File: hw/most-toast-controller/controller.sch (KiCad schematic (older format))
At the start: 1 part

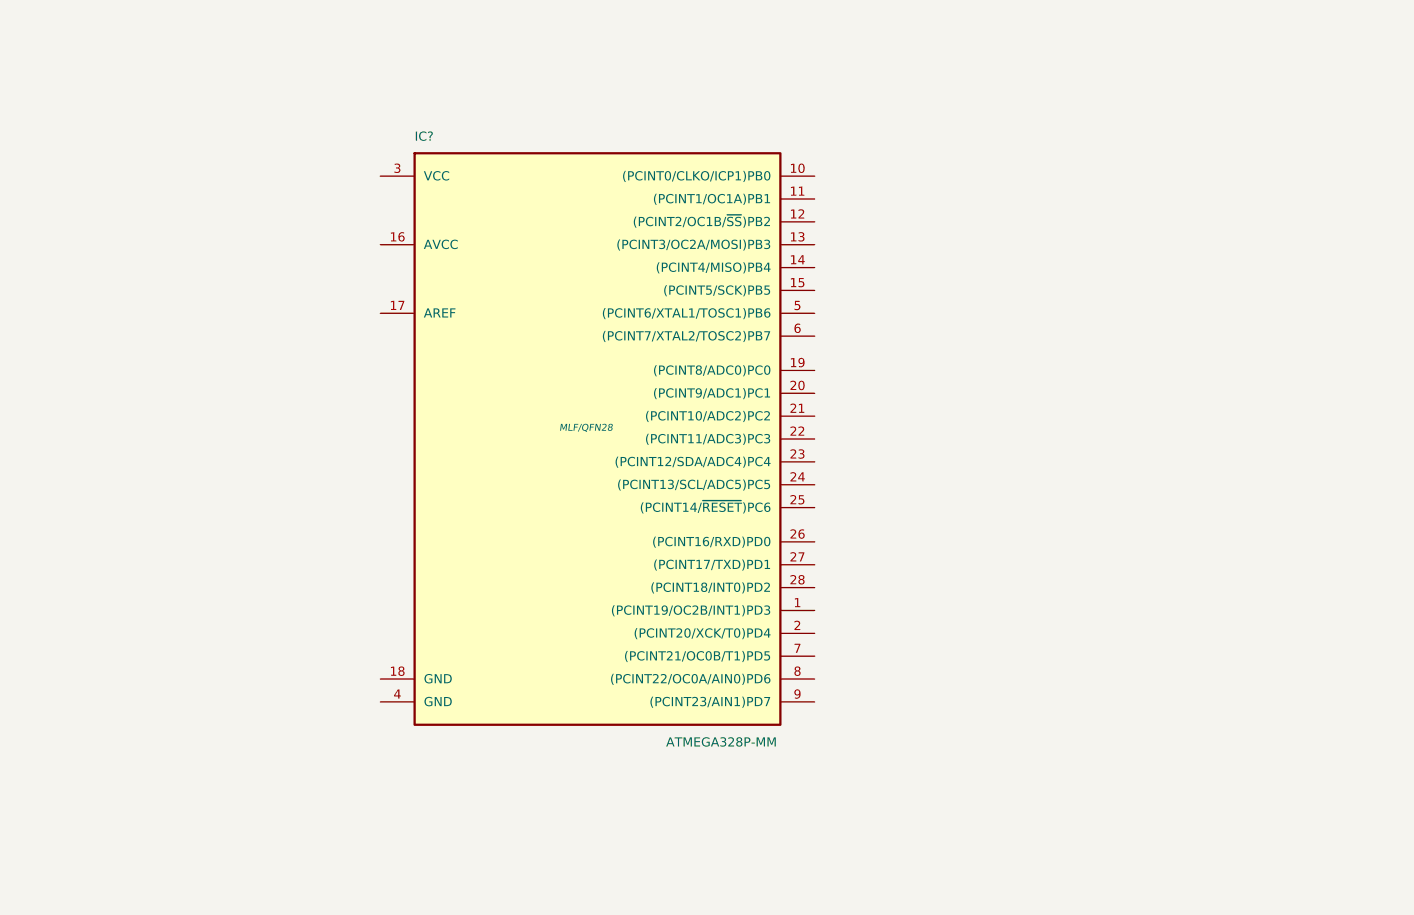
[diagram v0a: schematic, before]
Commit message: most-toast schematic finished.
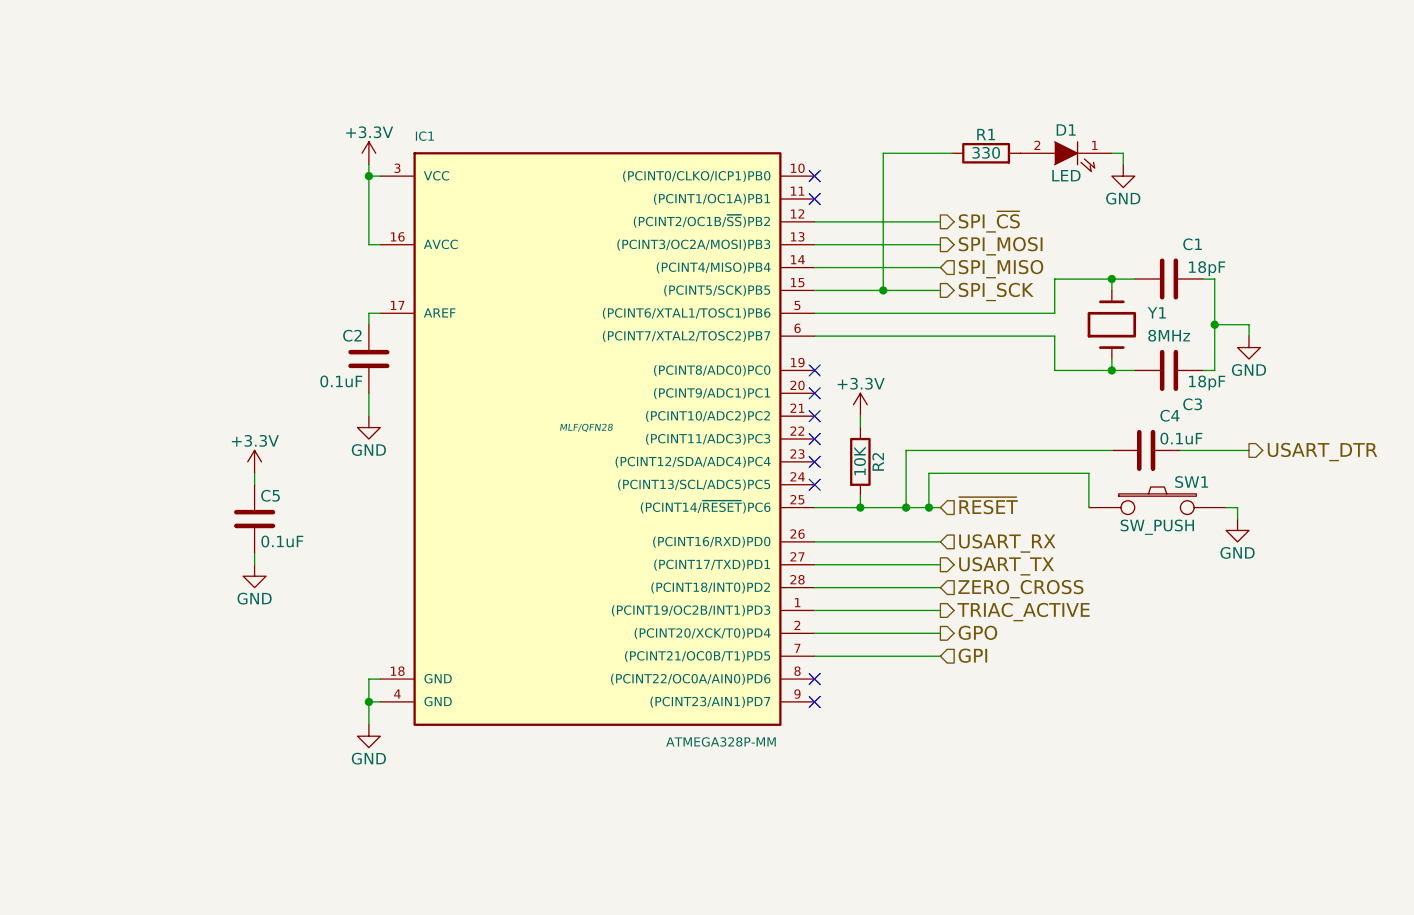
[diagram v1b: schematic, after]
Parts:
- added C1, C3: 18pF, symbol C
- added C2, C4, C5: 0.1uF, symbol C
- added D1: LED, symbol LED
- added R1: 330, symbol R
- added R2: 10K, symbol R
- added SW1: SW_PUSH, symbol SW_PUSH
- added Y1: 8MHz, symbol Crystal
- gave numbers to parts that had none: 1
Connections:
- net TRIAC_ACTIVE: now reaches IC1.1 ((PCINT19/OC2B/INT1)PD3)
- net SPI_~CS: now reaches IC1.12 ((PCINT2/OC1B/~SS~)PB2)
- net SPI_MOSI: now reaches IC1.13 ((PCINT3/OC2A/MOSI)PB3)
- net SPI_MISO: now reaches IC1.14 ((PCINT4/MISO)PB4)
- net SPI_SCK: now reaches IC1.15 ((PCINT5/SCK)PB5)
- net SPI_SCK: now also R1.1
- net +3V3: now reaches IC1.16 (AVCC)
- net +3V3: now also IC1.3 (VCC), C5.1, R2.1
- net at IC1.17 (AREF): now also C2.1
- net GND: now reaches IC1.18 (GND)
- net GND: now also IC1.4 (GND), C1.2, C2.2, C3.2, C5.2, D1.1 (K), SW1.2
- net GPO: now reaches IC1.2 ((PCINT20/XCK/T0)PD4)
- net ~RESET: now reaches IC1.25 ((PCINT14/~RESET~)PC6)
- net ~RESET: now also C4.1, R2.2, SW1.1
- net USART_RX: now reaches IC1.26 ((PCINT16/RXD)PD0)
- net USART_TX: now reaches IC1.27 ((PCINT17/TXD)PD1)
- net ZERO_CROSS: now reaches IC1.28 ((PCINT18/INT0)PD2)
- net at IC1.5 ((PCINT6/XTAL1/TOSC1)PB6): now also C1.1, Y1.2
- net at IC1.6 ((PCINT7/XTAL2/TOSC2)PB7): now also C3.1, Y1.1
- net GPI: now reaches IC1.7 ((PCINT21/OC0B/T1)PD5)
- new net: D1.2 (A), R1.2
- new net USART_DTR: C4.2
- no-connect marks 0 -> 10

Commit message: started putting most-toast on a board. Turns out one inch makes for very very small PCB
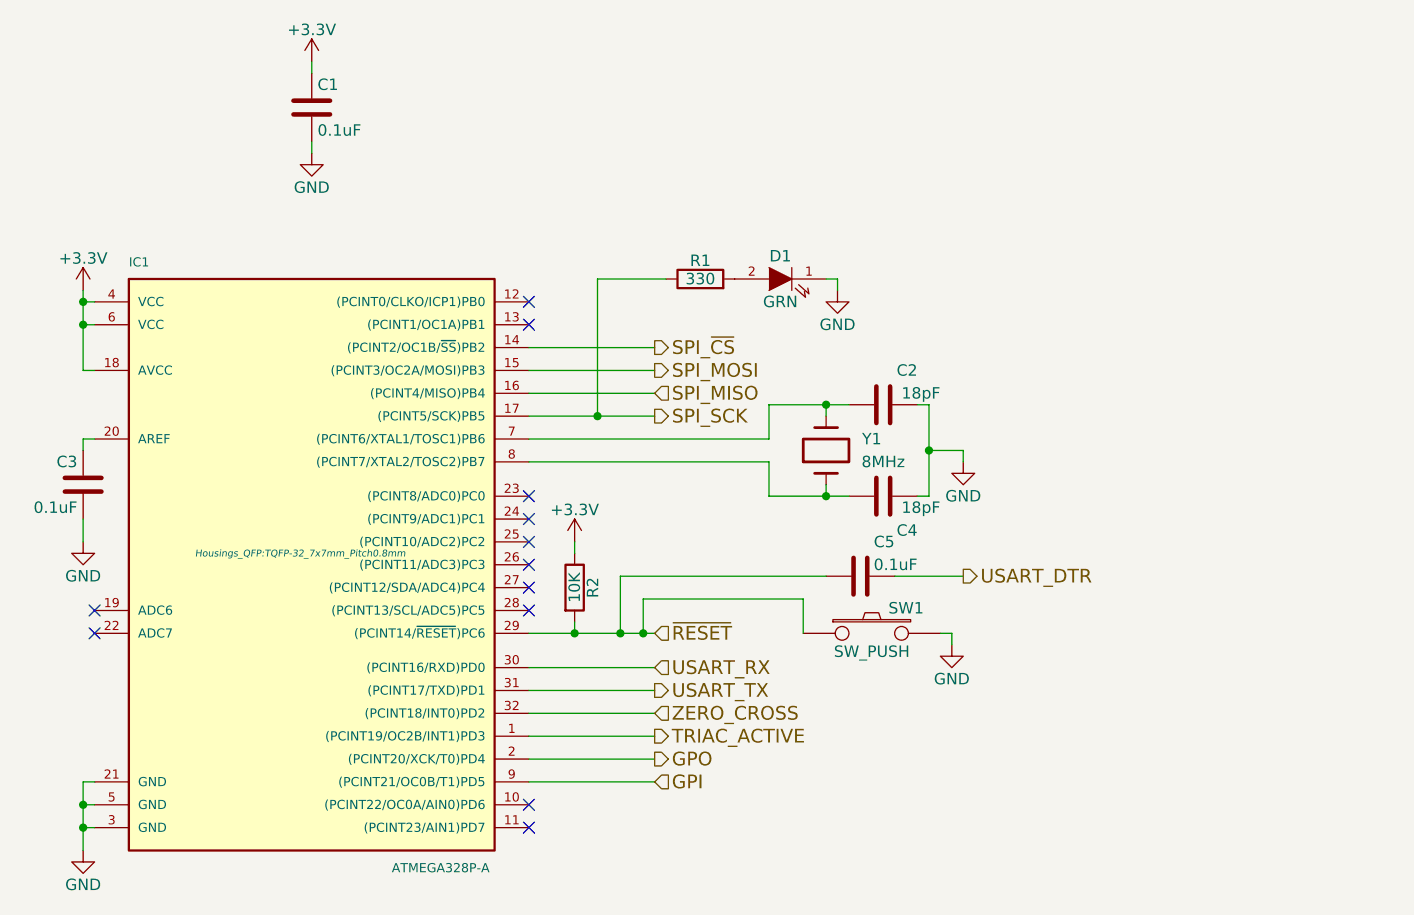
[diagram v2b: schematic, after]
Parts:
- removed IC1: ATMEGA328P-MM, MLF/QFN28, symbol ATMEGA328P-MM
- added IC1: ATMEGA328P-A, Housings_QFP:TQFP-32_7x7mm_Pitch0.8mm, symbol ATMEGA328P-A
- C1: renamed from C5; footprint (none) -> Capacitors_SMD:C_0805_HandSoldering
- C2: renamed from C1; footprint (none) -> Capacitors_SMD:C_0805_HandSoldering
- C3: renamed from C2; footprint (none) -> Capacitors_SMD:C_0805_HandSoldering
- C4: renamed from C3; footprint (none) -> Capacitors_SMD:C_0805_HandSoldering
- C5: renamed from C4; footprint (none) -> Capacitors_SMD:C_0805_HandSoldering
- D1: value LED -> GRN; footprint (none) -> Resistors_SMD:R_0805_HandSoldering
- R1, R2: footprint (none) -> Resistors_SMD:R_0805_HandSoldering
- SW1: footprint (none) -> Buttons_Switches_SMD:SW_SPST_FSMSM
- Y1: footprint (none) -> Crystals:Crystal_HC49-SD_SMD
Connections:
- net +3V3: now also IC1.18 (AVCC), IC1.4 (VCC), IC1.6 (VCC)
- net GND: now also IC1.21 (GND), IC1.3 (GND), IC1.5 (GND)
- net GPI: now also IC1.9 ((PCINT21/OC0B/T1)PD5)
- net GPO: now also IC1.2 ((PCINT20/XCK/T0)PD4)
- net SPI_MISO: now also IC1.16 ((PCINT4/MISO)PB4)
- net SPI_MOSI: now also IC1.15 ((PCINT3/OC2A/MOSI)PB3)
- net SPI_SCK: now also IC1.17 ((PCINT5/SCK)PB5)
- net SPI_~CS: now also IC1.14 ((PCINT2/OC1B/~SS~)PB2)
- net TRIAC_ACTIVE: now also IC1.1 ((PCINT19/OC2B/INT1)PD3)
- net USART_RX: now also IC1.30 ((PCINT16/RXD)PD0)
- net USART_TX: now also IC1.31 ((PCINT17/TXD)PD1)
- net ZERO_CROSS: now also IC1.32 ((PCINT18/INT0)PD2)
- net ~RESET: now also IC1.29 ((PCINT14/~RESET~)PC6)
- net at C3.1: now also IC1.20 (AREF)
- net at C2.1, Y1.2: now also IC1.7 ((PCINT6/XTAL1/TOSC1)PB6)
- net at C4.1, Y1.1: now also IC1.8 ((PCINT7/XTAL2/TOSC2)PB7)
- no-connect marks 10 -> 12
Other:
- moved on the sheet: C1, C2, C3, C4, C5, D1, R1, R2, SW1, Y1
